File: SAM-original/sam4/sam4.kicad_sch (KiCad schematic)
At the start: 0 parts

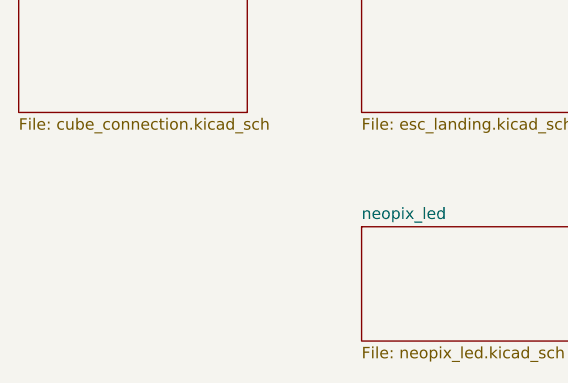
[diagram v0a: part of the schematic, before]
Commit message: finalize core routing
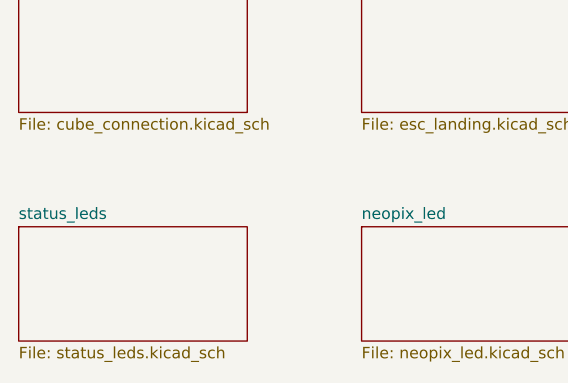
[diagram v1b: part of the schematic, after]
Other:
- added sheet status_leds (status_leds.kicad_sch)
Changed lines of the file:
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@@
+	)
+	(sheet
+		(at 50.8 63.5)
+		(size 25.4 12.7)
+		(exclude_from_sim no)
+		(in_bom yes)
+		(on_board yes)
+		(dnp no)
+		(fields_autoplaced yes)
+		(stroke
+			(width 0.1524)
+			(type solid)
+		)
+		(fill
+			(color 0 0 0 0.0000)
+		)
+		(property "Sheetname" "status_leds"
+			(at 50.8 62.7884 0)
+			(effects
+				(font
+					(size 1.27 1.27)
+				)
+				(justify left bottom)
+			)
+		)
+		(property "Sheetfile" "status_leds.kicad_sch"
+			(at 50.8 76.7846 0)
+			(effects
+				(font
+					(size 1.27 1.27)
+				)
+				(justify left top)
+			)
+		)
+		(instances
+			(project "sam4"
+				(path "/01aa8038-f16d-42dc-9377-7a3d64116781"
+					(page "8")
+				)
+			)
+		)
 	)
 	(sheet

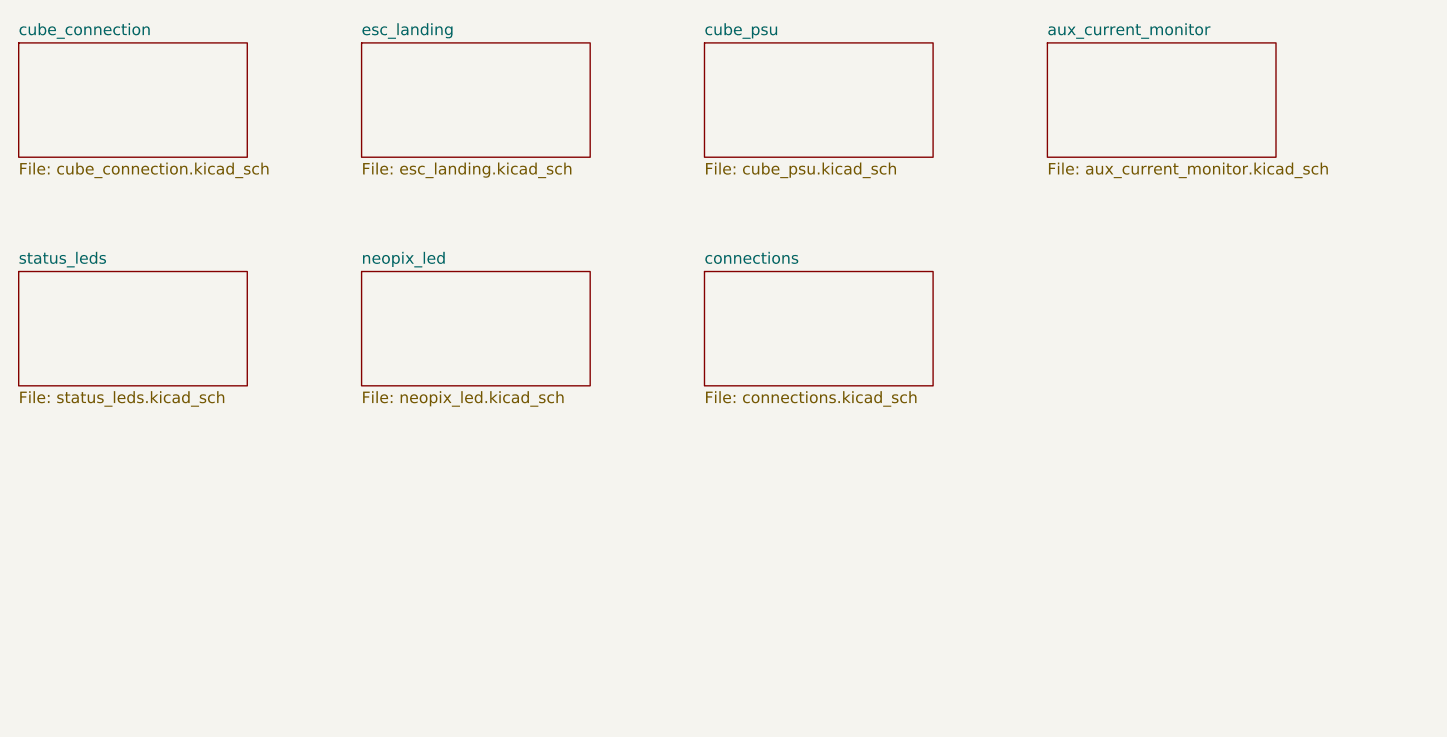
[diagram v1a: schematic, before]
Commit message: add updated SAM4 routing (DRC clean) + model
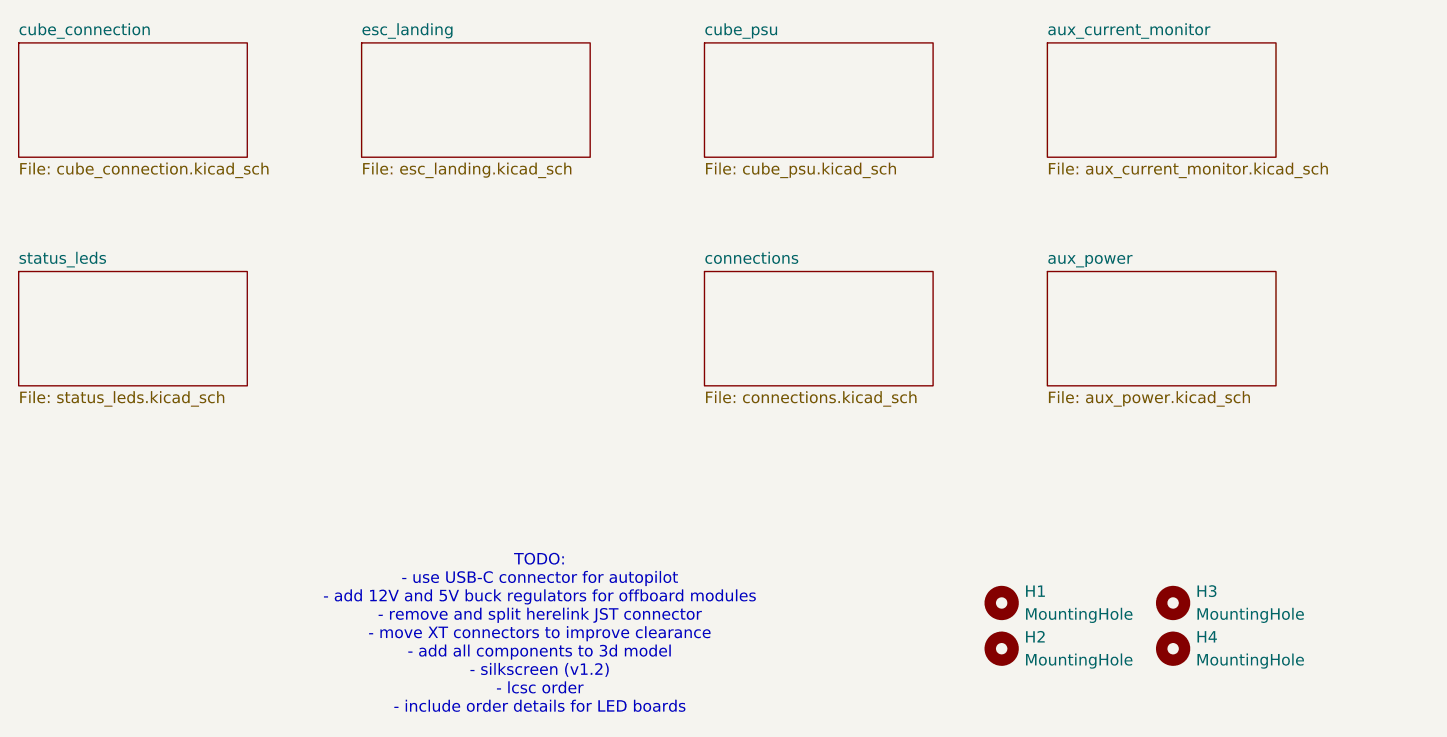
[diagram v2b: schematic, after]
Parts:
- added H1, H2, H3, H4: MountingHole, MountingHole:MountingHole_3.2mm_M3_DIN965, symbol Mechanical:MountingHole
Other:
- removed sheet neopix_led
- added sheet aux_power (aux_power.kicad_sch)
- note added: "TODO: - use USB-C connector for autopilot - add 12V and 5V buck regulators for offboard modules - remove and split herelink JST connector - move XT connectors to improve clearance - add all components to 3d model - silkscreen (v1.2) - lcsc order - include order details for LED boards"
